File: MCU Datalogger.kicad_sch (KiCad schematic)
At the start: 24 parts

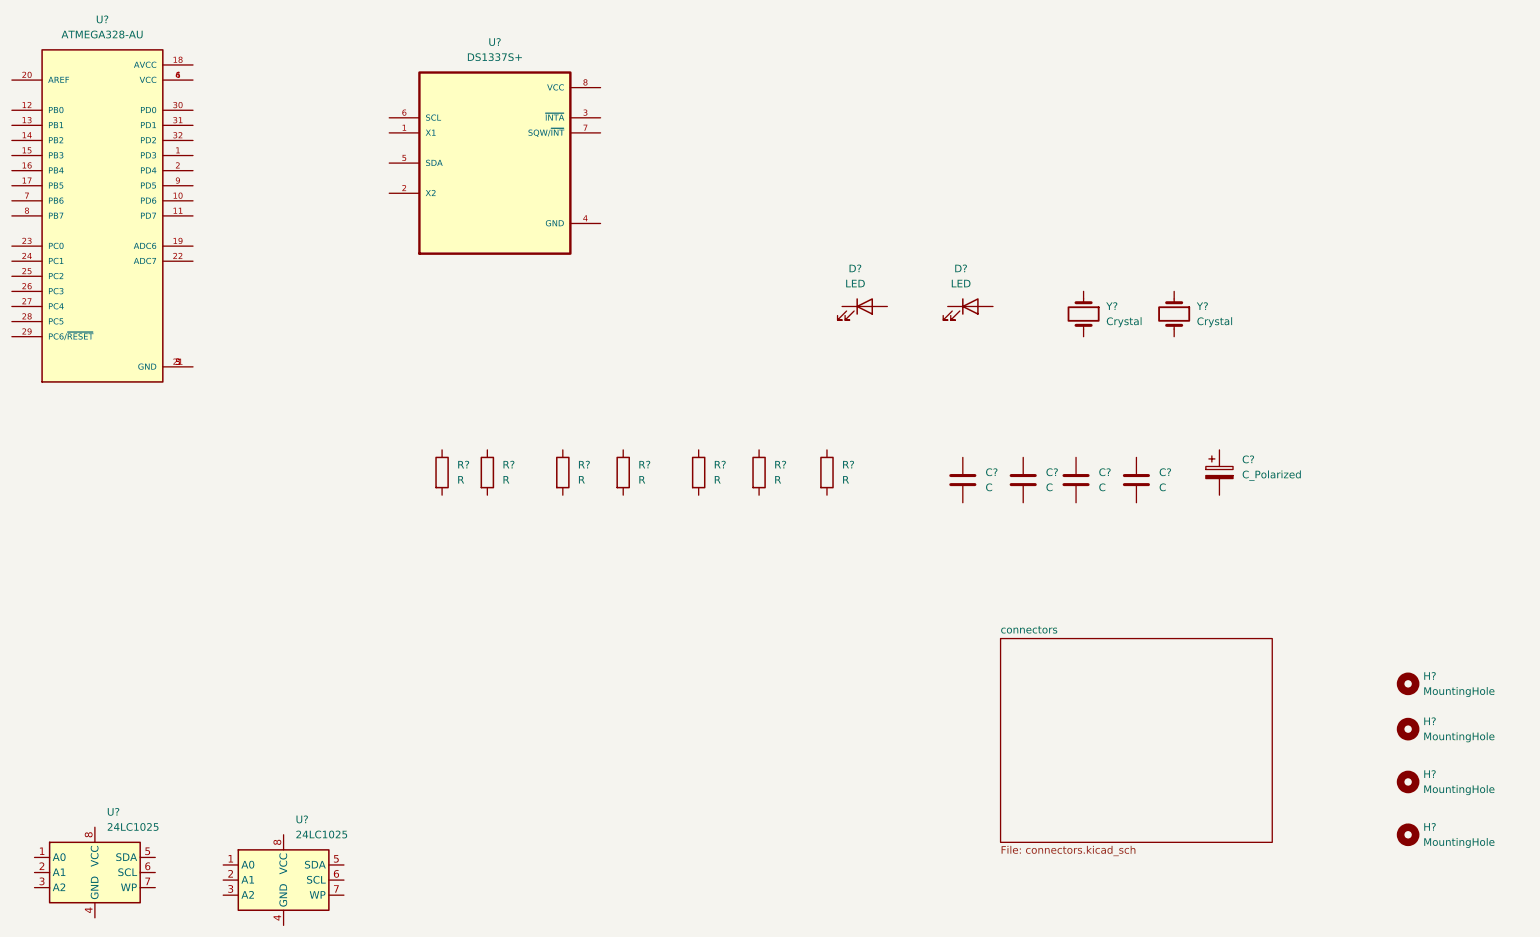
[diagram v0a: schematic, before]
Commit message: Place the symbols at relevent place.(Arrange) and Annote them.
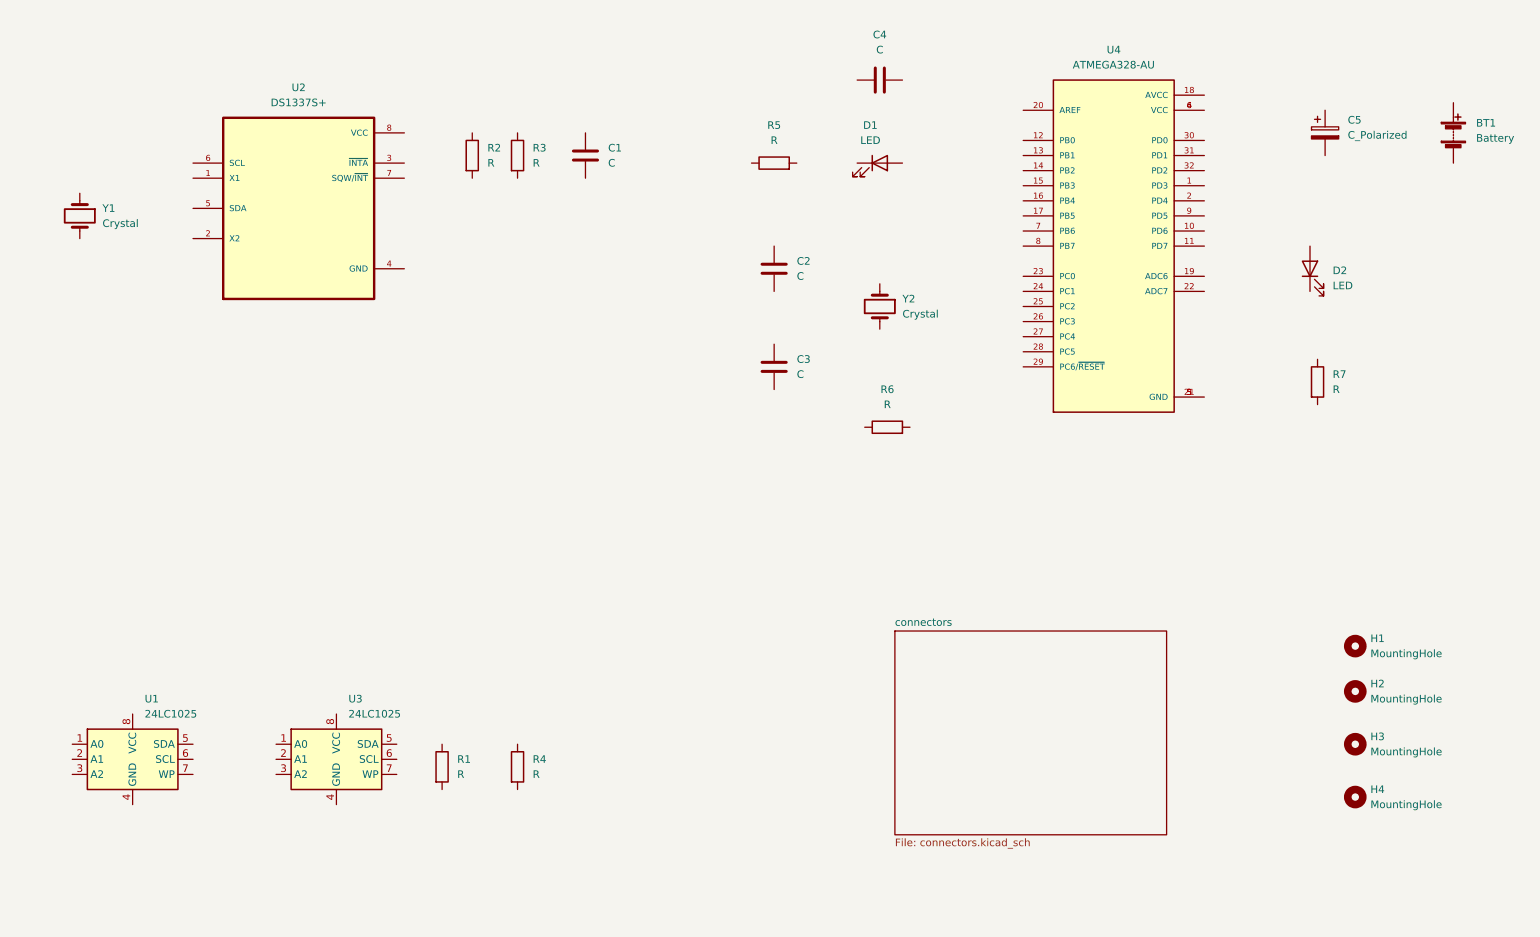
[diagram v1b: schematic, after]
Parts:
- added BT1: Battery, symbol Device:Battery
- gave numbers to parts that had none: 24
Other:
- moved on the sheet: C1, C2, C3, C4, C5, D1, D2, H1, H2, H3, H4, R1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

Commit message: Added component(symbol) Values.
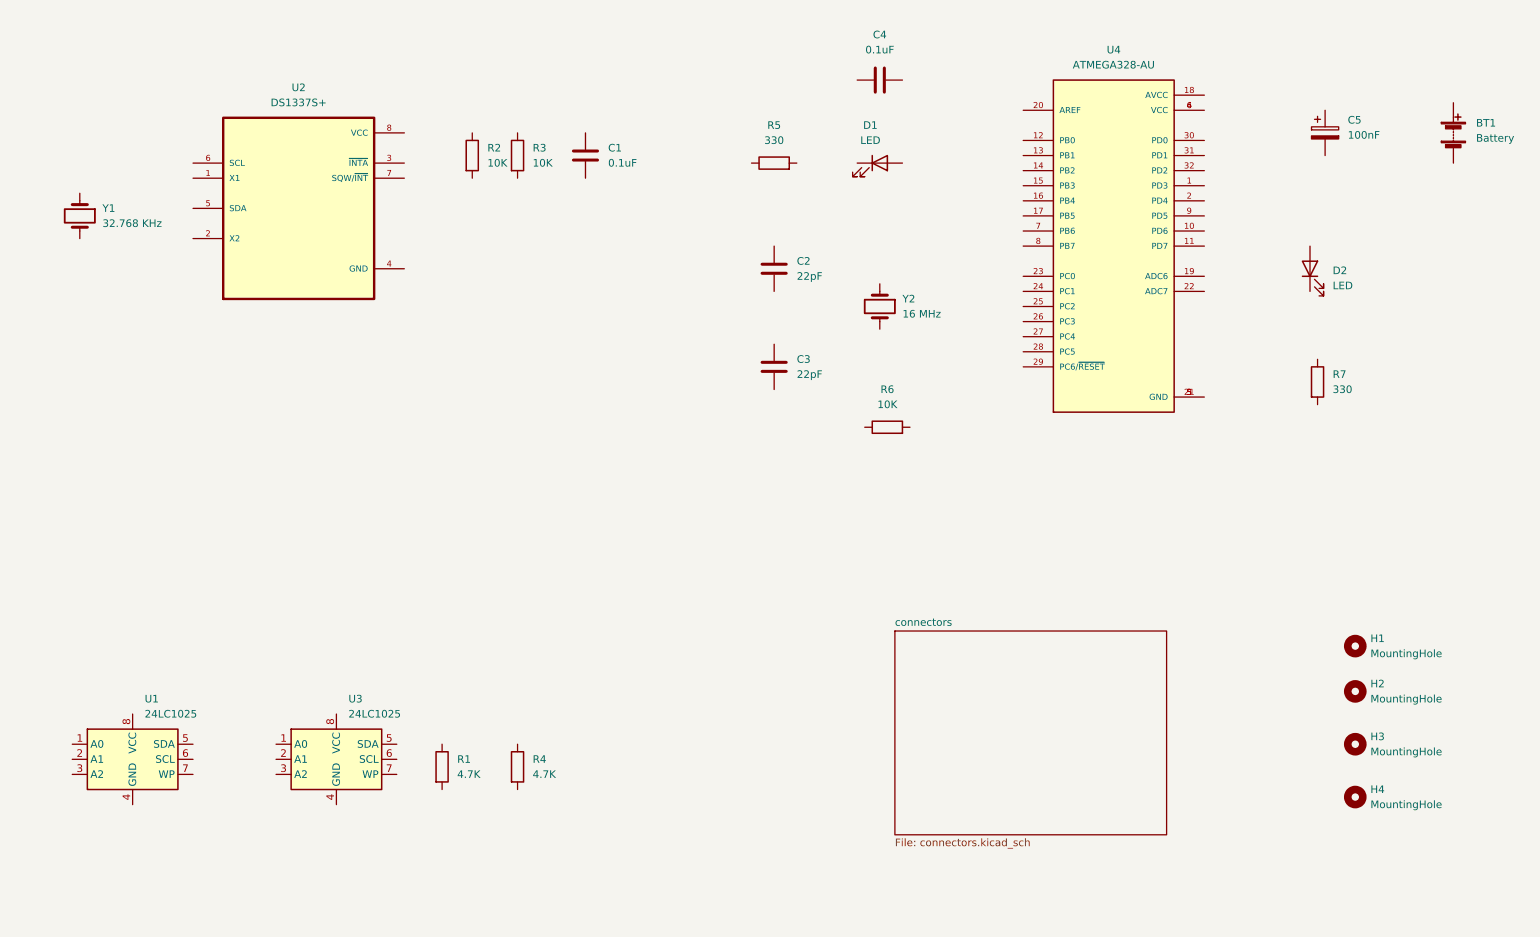
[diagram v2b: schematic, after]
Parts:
- C1, C4: value C -> 0.1uF
- C2, C3: value C -> 22pF
- C5: value C_Polarized -> 100nF
- R1, R4: value R -> 4.7K
- R2, R3, R6: value R -> 10K
- R5, R7: value R -> 330
- Y1: value Crystal -> 32.768 KHz
- Y2: value Crystal -> 16 MHz
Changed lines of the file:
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@@
       (effects (font (size 1.27 1.27)) (justify left))
     )
-    (property "Value" "R" (id 1) (at 116.84 149.8599 0)
+    (property "Value" "4.7K" (id 1) (at 116.84 149.8599 0)
       (effects (font (size 1.27 1.27)) (justify left))
     )
@@
       (effects (font (size 1.27 1.27)) (justify left))
     )
-    (property "Value" "R" (id 1) (at 104.14 149.8599 0)
+    (property "Value" "4.7K" (id 1) (at 104.14 149.8599 0)
       (effects (font (size 1.27 1.27)) (justify left))
     )
@@
       (effects (font (size 1.27 1.27)) (justify left))
     )
-    (property "Value" "R" (id 1) (at 116.84 46.9899 0)
+    (property "Value" "10K" (id 1) (at 116.84 46.9899 0)
       (effects (font (size 1.27 1.27)) (justify left))
     )
@@
       (effects (font (size 1.27 1.27)) (justify left))
     )
-    (property "Value" "C" (id 1) (at 161.29 66.0399 0)
+    (property "Value" "22pF" (id 1) (at 161.29 66.0399 0)
       (effects (font (size 1.27 1.27)) (justify left))
     )
@@
     (in_bom yes) (on_board yes) (fields_autoplaced)
     (property "Reference" "C4" (id 0) (at 175.26 25.4 90))
-    (property "Value" "C" (id 1) (at 175.26 27.94 90))
+    (property "Value" "0.1uF" (id 1) (at 175.26 27.94 90))
     (property "Footprint" "" (id 2) (at 179.07 32.0548 0)
       (effects (font (size 1.27 1.27)) hide)
@@
       (effects (font (size 1.27 1.27)) (justify left))
     )
-    (property "Value" "Crystal" (id 1) (at 44.45 57.1499 90)
+    (property "Value" "32.768 KHz" (id 1) (at 44.45 57.1499 90)
       (effects (font (size 1.27 1.27)) (justify left))
     )
@@
       (effects (font (size 1.27 1.27)) (justify left))
     )
-    (property "Value" "C_Polarized" (id 1) (at 254 42.2909 0)
+    (property "Value" "100nF" (id 1) (at 254 42.2909 0)
       (effects (font (size 1.27 1.27)) (justify left))
     )
@@
     (in_bom yes) (on_board yes) (fields_autoplaced)
     (property "Reference" "R6" (id 0) (at 176.53 85.09 90))
-    (property "Value" "R" (id 1) (at 176.53 87.63 90))
+    (property "Value" "10K" (id 1) (at 176.53 87.63 90))
     (property "Footprint" "" (id 2) (at 176.53 93.218 90)
       (effects (font (size 1.27 1.27)) hide)
@@
       (effects (font (size 1.27 1.27)) (justify left))
     )
-    (property "Value" "R" (id 1) (at 109.22 46.9899 0)
+    (property "Value" "10K" (id 1) (at 109.22 46.9899 0)
       (effects (font (size 1.27 1.27)) (justify left))
     )
@@
       (effects (font (size 1.27 1.27)) (justify left))
     )
-    (property "Value" "R" (id 1) (at 251.46 85.0899 0)
+    (property "Value" "330" (id 1) (at 251.46 85.0899 0)
       (effects (font (size 1.27 1.27)) (justify left))
     )
@@
       (effects (font (size 1.27 1.27)) (justify left))
     )
-    (property "Value" "C" (id 1) (at 129.54 46.9899 0)
+    (property "Value" "0.1uF" (id 1) (at 129.54 46.9899 0)
       (effects (font (size 1.27 1.27)) (justify left))
     )
@@
       (effects (font (size 1.27 1.27)) (justify left))
     )
-    (property "Value" "Crystal" (id 1) (at 179.07 72.3899 90)
+    (property "Value" "16 MHz" (id 1) (at 179.07 72.3899 90)
       (effects (font (size 1.27 1.27)) (justify left))
     )
@@
       (effects (font (size 1.27 1.27)) (justify left))
     )
-    (property "Value" "C" (id 1) (at 161.29 82.5499 0)
+    (property "Value" "22pF" (id 1) (at 161.29 82.5499 0)
       (effects (font (size 1.27 1.27)) (justify left))
     )
@@
     (in_bom yes) (on_board yes) (fields_autoplaced)
     (property "Reference" "R5" (id 0) (at 157.48 40.64 90))
-    (property "Value" "R" (id 1) (at 157.48 43.18 90))
+    (property "Value" "330" (id 1) (at 157.48 43.18 90))
     (property "Footprint" "" (id 2) (at 157.48 48.768 90)
       (effects (font (size 1.27 1.27)) hide)
@@
     )
     (path "/c7b012b6-1d80-4249-a76b-52a3e8bdaba6"
-      (reference "C1") (unit 1) (value "C") (footprint "")
+      (reference "C1") (unit 1) (value "0.1uF") (footprint "")
     )
     (path "/4a7424f8-fcfe-4cc9-8538-6331bc8d92ac"
-      (reference "C2") (unit 1) (value "C") (footprint "")
+      (reference "C2") (unit 1) (value "22pF") (footprint "")
     )
     (path "/d7fd3e9b-ca36-436c-99fe-84fe566620dc"
-      (reference "C3") (unit 1) (value "C") (footprint "")
+      (reference "C3") (unit 1) (value "22pF") (footprint "")
     )
     (path "/5ae0cbba-0dd3-423e-9c5a-66111e840640"
-      (reference "C4") (unit 1) (value "C") (footprint "")
+      (reference "C4") (unit 1) (value "0.1uF") (footprint "")
     )
     (path "/90e79933-18e6-433e-8d0a-16f77c5a56ce"
-      (reference "C5") (unit 1) (value "C_Polarized") (footprint "")
+      (reference "C5") (unit 1) (value "100nF") (footprint "")
     )
     (path "/bbe6bdca-0b46-4be2-8673-ed1b722fb8bd"
@@
     )
     (path "/3803b2ce-7e9a-40a0-b4c9-38bd610cce6c"
-      (reference "R1") (unit 1) (value "R") (footprint "")
+      (reference "R1") (unit 1) (value "4.7K") (footprint "")
     )
     (path "/be558577-e443-4e86-a8e5-711a0bae3949"
-      (reference "R2") (unit 1) (value "R") (footprint "")
+      (reference "R2") (unit 1) (value "10K") (footprint "")
     )
     (path "/44a3c8d0-66ac-477d-80c1-be2ec7c65d22"
-      (reference "R3") (unit 1) (value "R") (footprint "")
+      (reference "R3") (unit 1) (value "10K") (footprint "")
     )
     (path "/0449299b-9326-4bc1-8c4a-33c4ada761e9"
-      (reference "R4") (unit 1) (value "R") (footprint "")
+      (reference "R4") (unit 1) (value "4.7K") (footprint "")
     )
     (path "/e50b4c61-211b-432d-b71f-6c7299679088"
-      (reference "R5") (unit 1) (value "R") (footprint "")
+      (reference "R5") (unit 1) (value "330") (footprint "")
     )
     (path "/b633b1ae-1bed-41da-8bf7-13f94cd2b0b7"
-      (reference "R6") (unit 1) (value "R") (footprint "")
+      (reference "R6") (unit 1) (value "10K") (footprint "")
     )
     (path "/c489e95f-80ec-4b0b-9d7f-7b05088cb37d"
-      (reference "R7") (unit 1) (value "R") (footprint "")
+      (reference "R7") (unit 1) (value "330") (footprint "")
     )
     (path "/48c06b6f-c7ea-48ef-9fdd-8a2f270f6649"
@@
     )
     (path "/6071aefe-fb18-4a31-addc-61ccbab2daf6"
-      (reference "Y1") (unit 1) (value "Crystal") (footprint "")
+      (reference "Y1") (unit 1) (value "32.768 KHz") (footprint "")
     )
     (path "/c94e30dc-95fd-47a0-8178-2b2c90a10608"
-      (reference "Y2") (unit 1) (value "Crystal") (footprint "")
-    )
-  )
+      (reference "Y2") (unit 1) (value "16 MHz") (footprint "")
+    )
+  )

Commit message: Done with the symbol-footprint associations
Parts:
- BT1: footprint (none) -> Connector_PinHeader_2.54mm:PinHeader_1x02_P2.54mm_Vertical
- C1, C2, C3, C4, C5: footprint (none) -> Capacitor_SMD:C_0805_2012Metric
- D1, D2: footprint (none) -> LED_SMD:LED_0805_2012Metric
- H1, H2, H3, H4: footprint (none) -> MountingHole:MountingHole_2.1mm
- R1, R2, R3, R4, R5, R6, R7: footprint (none) -> Resistor_SMD:R_0805_2012Metric
- U1, U3: footprint (none) -> Package_SO:SOIC-8_5.23x5.23mm_P1.27mm
- U2: footprint SOIC127P600X175-8N -> Footprints:SOIC127P600X175-8N
- U4: footprint QFP80P900X900X120-32N -> Footprints:QFP80P900X900X120-32N
- Y1, Y2: footprint (none) -> Crystal:Crystal_SMD_5032-2Pin_5.0x3.2mm_HandSoldering
